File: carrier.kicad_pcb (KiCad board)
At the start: 4 copper layers, 20.3 x 68.6 mm, 29 parts, among them J1 Conn_02x06_Odd_Even, J2 Conn_01x26, J3 Conn_01x26, U1 CARAVEL, U2 W25Q128JVS, U3 LP5907MFX-3.3, U4 LP5907MFX-1.8, U5 LP5907MFX-1.8, U6 LP5907MFX-3.3, X1 SG-5032CAN

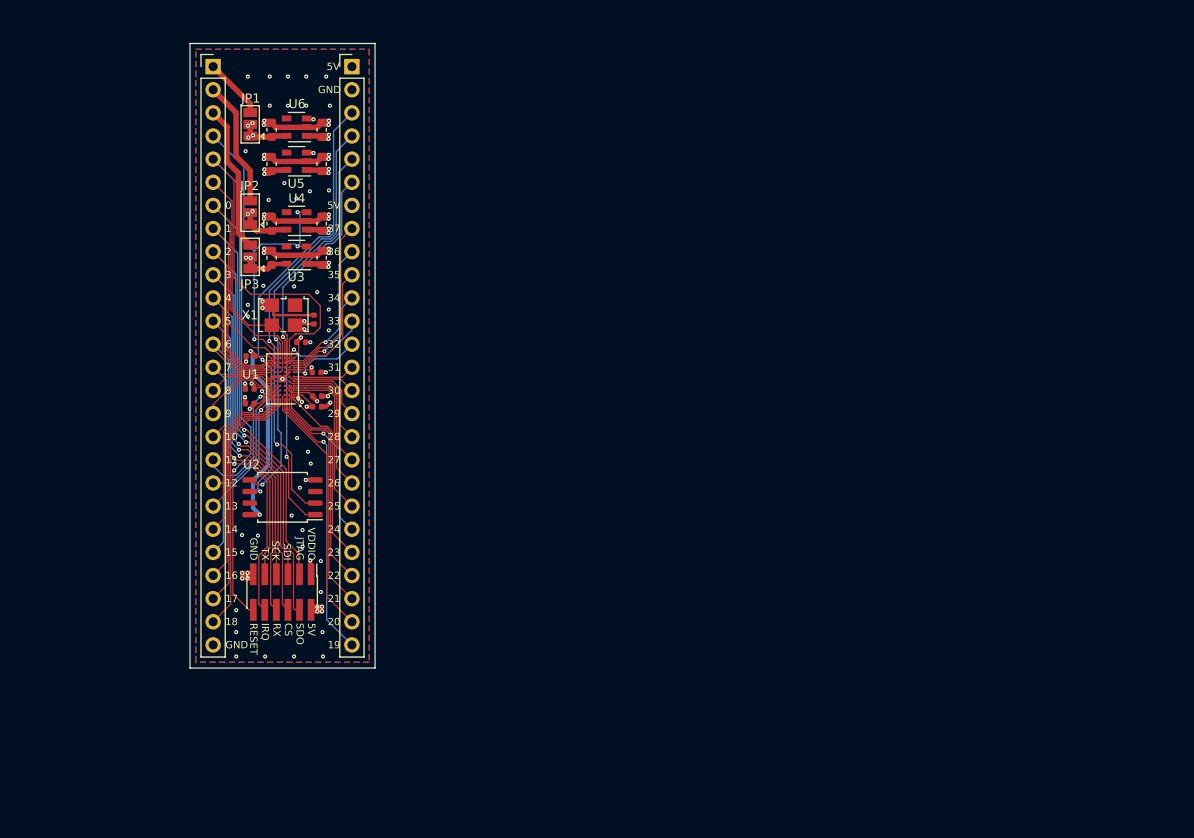
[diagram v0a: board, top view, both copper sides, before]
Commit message: Switch to 2.54mm header for programming
Also imports changes from schematic to PCB.
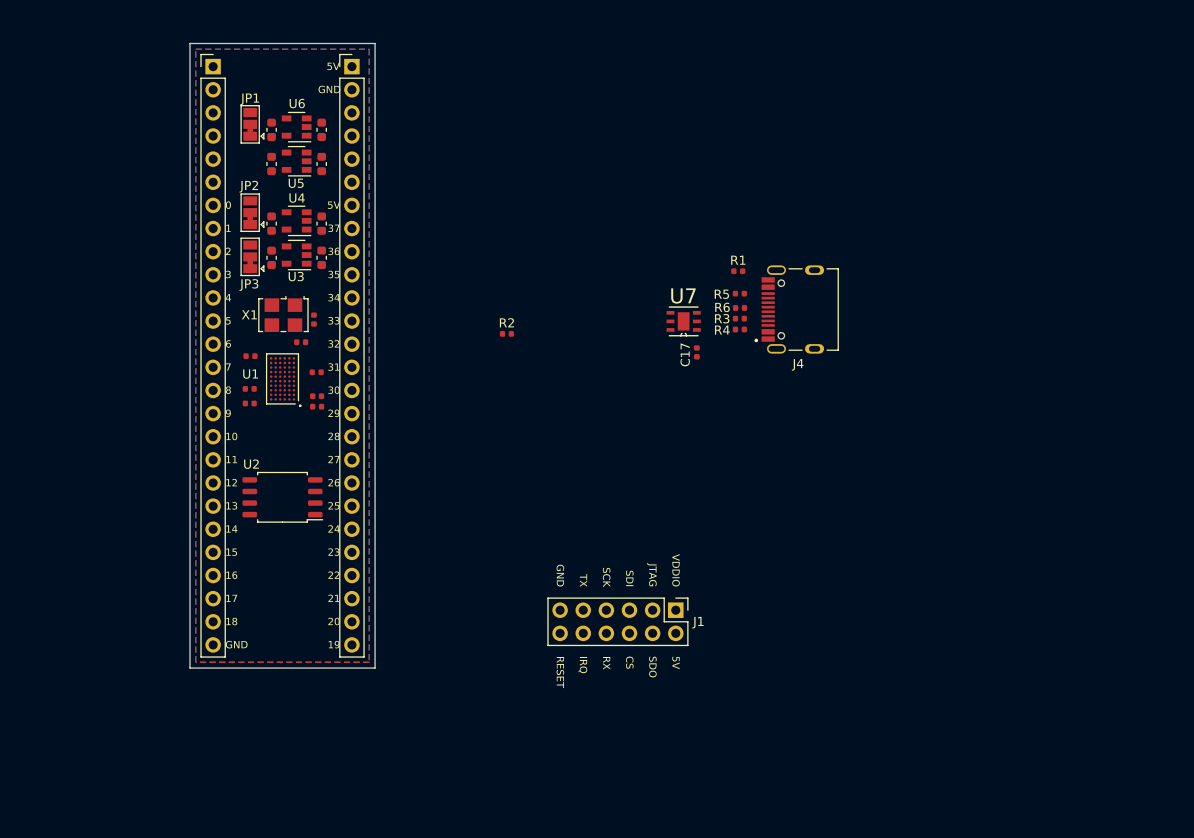
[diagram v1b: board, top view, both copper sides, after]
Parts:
- added C17: 22n, Capacitor_SMD:C_0402_1005Metric, F.Cu at (114.2, 77.1)
- added J4: TYPE-C-31-M-12, HRO_TYPE-C-31-M-12:HRO_TYPE-C-31-M-12, F.Cu at (127.2, 72.4)
- added R1: 1M Ohm, Resistor_SMD:R_0402_1005Metric, F.Cu at (118.8, 68.2)
- added R2: 22 Ohm, Resistor_SMD:R_0402_1005Metric, F.Cu at (93.4, 75.1)
- added R3: 22 Ohm, Resistor_SMD:R_0402_1005Metric, F.Cu at (118.9, 73.4)
- added R4: 5k1 Ohm, Resistor_SMD:R_0402_1005Metric, F.Cu at (118.9, 74.6)
- added R5: 5k1 Ohm, Resistor_SMD:R_0402_1005Metric, F.Cu at (118.9, 70.6)
- added R6: 1.5k Ohm, Resistor_SMD:R_0402_1005Metric, F.Cu at (119.0, 72.2)
- added U7: TPD2E001DRSR, TPD2E001DRSR:SON95P315X315X80-7N, F.Cu at (112.8, 73.7)
- J1: footprint Connector_PinHeader_1.27mm:PinHeader_2x06_P1.27mm_Vertical_SMD -> Connector_PinHeader_2.54mm:PinHeader_2x06_P2.54mm_Vertical
- moved J1 43.3 mm to (111.9, 105.4)
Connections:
- U1 pad D3: mprj_io[13] -> usb_pu
- U1 pad E3: mprj_io[11] -> usb_dn
- U1 pad F3: mprj_io[12] -> usb_dp
- U2 pad 3: no_connect_58 -> unconnected-(U2-Pad3)
- U2 pad 7: no_connect_59 -> unconnected-(U2-Pad7)
- U3 pad 4: no_connect_60 -> unconnected-(U3-Pad4)
- U4 pad 4: no_connect_61 -> unconnected-(U4-Pad4)
- U5 pad 4: no_connect_62 -> unconnected-(U5-Pad4)
- U6 pad 4: no_connect_63 -> unconnected-(U6-Pad4)
- X1 pad 1: no_connect_64 -> unconnected-(X1-Pad1)
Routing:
- net +5V: track 93.3 -> 0.00 mm, vias 14 -> 0
- net resetb: track 86.3 -> 0.00 mm, vias 1 -> 0
- net vdda: track 76.0 -> 0.00 mm, vias 6 -> 0
- net mprj_io[0]: track 67.5 -> 0.00 mm, vias 1 -> 0
- net mprj_io[1]: track 64.7 -> 0.00 mm, vias 1 -> 0
- net GND: track 61.9 -> 0.00 mm, vias 74 -> 0
- net vddio: track 58.0 -> 0.00 mm, vias 4 -> 0
- net mprj_io[2]: track 56.0 -> 0.00 mm, vias 1 -> 0
- net mprj_io[3]: track 55.9 -> 0.00 mm, vias 1 -> 0
- net flash_clk: track 51.4 -> 0.00 mm, vias 2 -> 0
- net flash_io1: track 50.6 -> 0.00 mm, vias 2 -> 0
- net mprj_io[4]: track 46.2 -> 0.00 mm, vias 1 -> 0
- net mprj_io[5]: track 46.1 -> 0.00 mm, vias 1 -> 0
- net flash_io0: track 44.8 -> 0.00 mm, vias 2 -> 0
- net flash_csb: track 44.6 -> 0.00 mm, vias 2 -> 0
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
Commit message: Update caravel ASIC footprint
It was mirrored about the Y-axis.

Thanks to Tim Edwards and Matt Venn for flagging this issue.
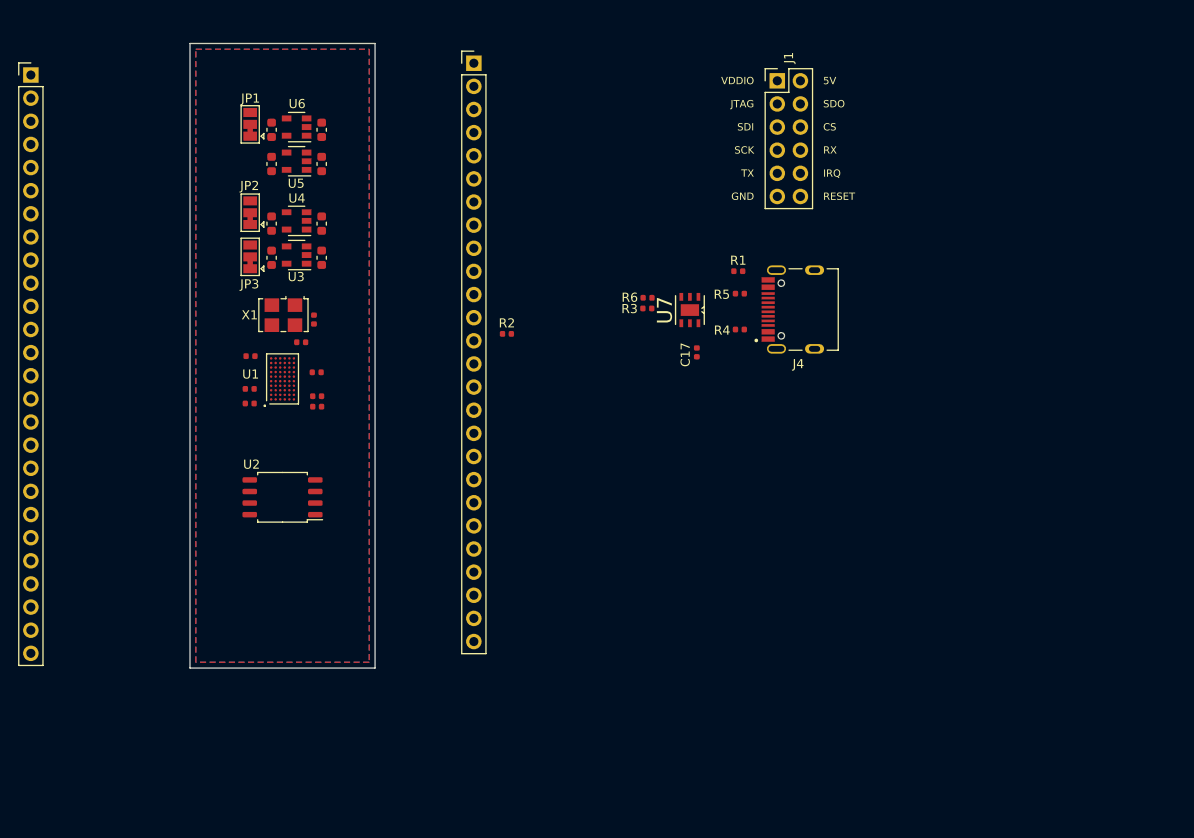
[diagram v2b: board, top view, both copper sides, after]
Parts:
- moved J1 59.2 mm to (123.1, 47.3), turned to 0 degrees
- moved J3 35.3 mm to (41.1, 46.6)
- moved J2 28.6 mm to (89.7, 45.3)
- moved R3 10.2 mm to (108.8, 72.3)
- moved R6 10.2 mm to (108.8, 71.1)
- moved U7 1.42 mm to (113.5, 72.4), turned to -90 degrees
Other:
- board text removed: "0"
- board text removed: "1"
- board text removed: "10"
- board text removed: "11"
- board text removed: "12"
- board text removed: "13"
- board text removed: "14"
- board text removed: "15"
- board text removed: "16"
- board text removed: "17"
- board text removed: "18"
- board text removed: "19"
- board text removed: "2"
- board text removed: "20"
- board text removed: "21"
- board text removed: "22"
- board text removed: "23"
- board text removed: "24"
- board text removed: "25"
- board text removed: "26"
- board text removed: "27"
- board text removed: "28"
- board text removed: "29"
- board text removed: "3"
- board text removed: "30"
- board text removed: "31"
- board text removed: "32"
- board text removed: "33"
- board text removed: "34"
- board text removed: "35"
- board text removed: "36"
- board text removed: "37"
- board text removed: "4"
- board text removed: "5"
- board text removed: "6"
- board text removed: "7"
- board text removed: "8"
- board text removed: "9"

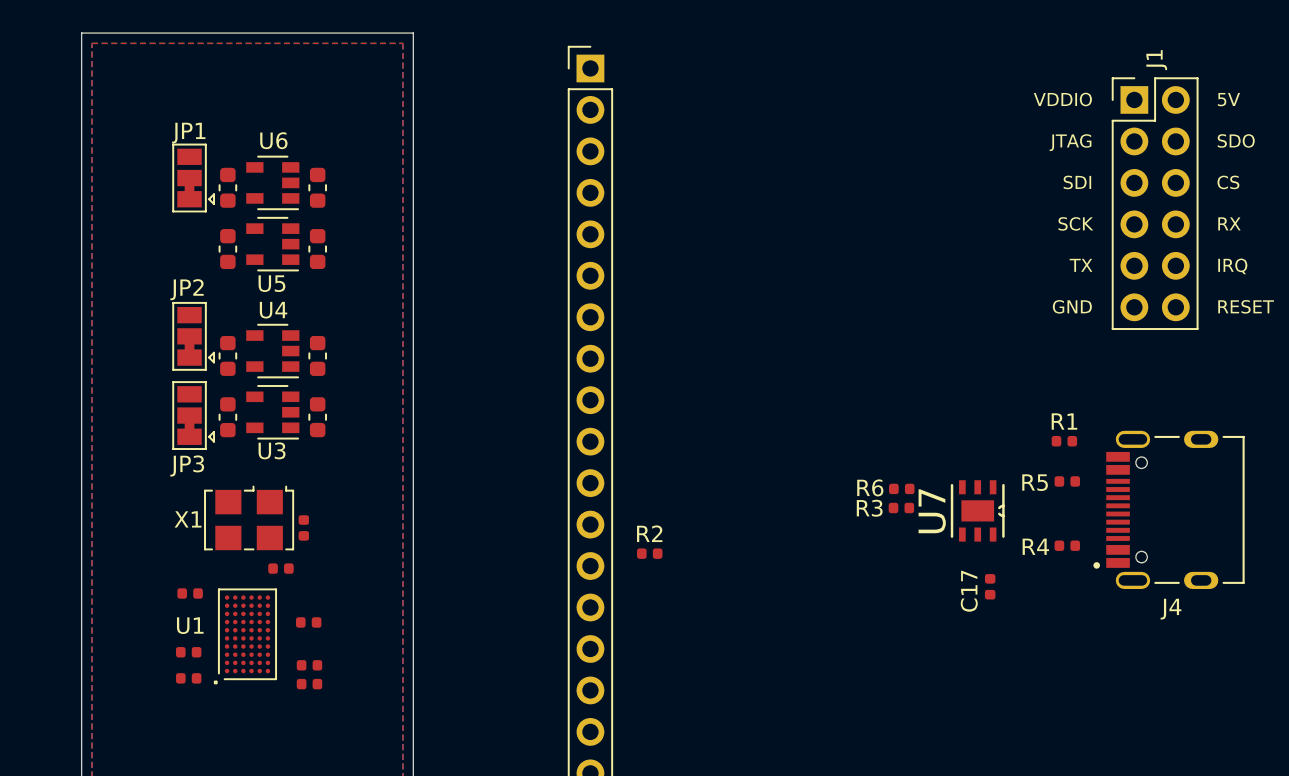
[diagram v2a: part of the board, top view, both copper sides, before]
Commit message: Add current measurement jumpers
Removes solder bridges and adds jumpers for each power rail to measure current.
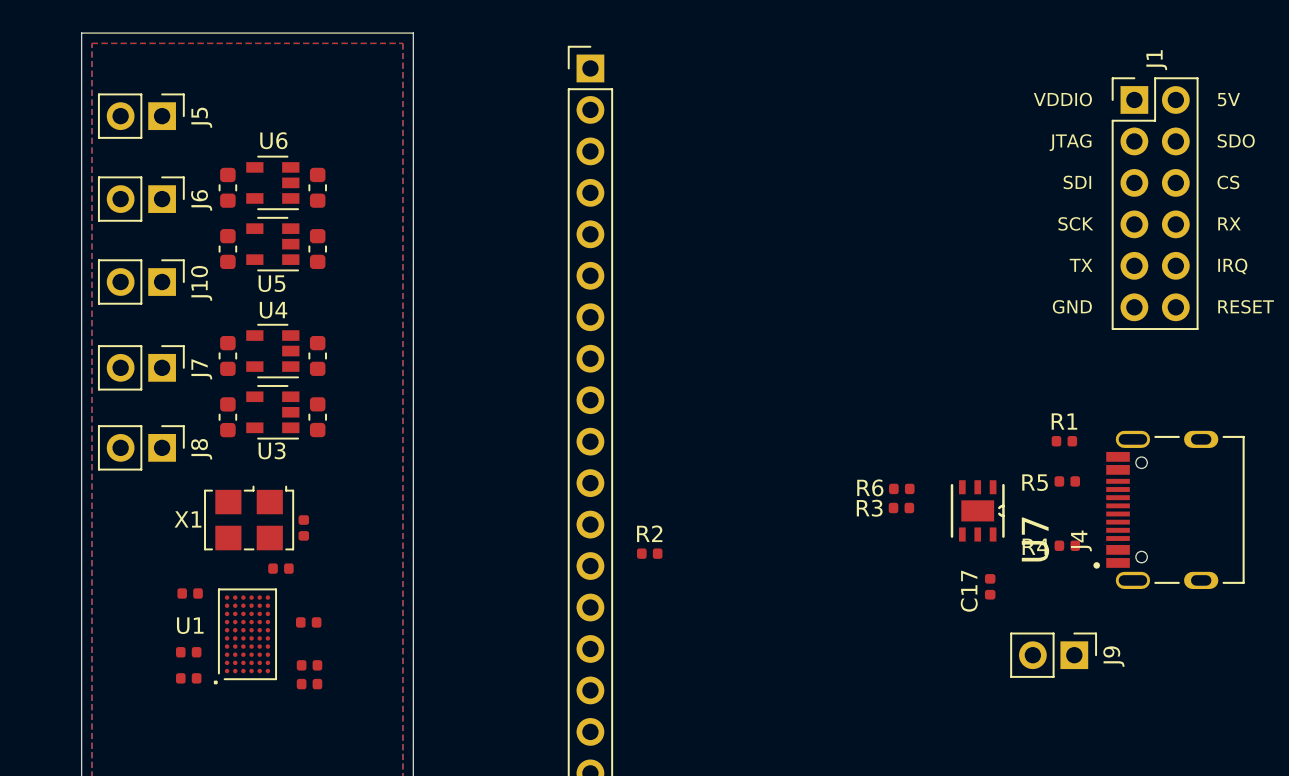
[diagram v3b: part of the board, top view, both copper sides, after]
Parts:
- removed JP1: VIO_SEL, Jumper:SolderJumper-3_P1.3mm_Bridged12_Pad1.0x1.5mm
- removed JP2: 1V8_SEL, Jumper:SolderJumper-3_P1.3mm_Bridged12_Pad1.0x1.5mm
- removed JP3: 3V3_SEL, Jumper:SolderJumper-3_P1.3mm_Bridged12_Pad1.0x1.5mm
- added J10: Conn_01x02, Connector_PinHeader_2.54mm:PinHeader_1x02_P2.54mm_Vertical, F.Cu at (63.5, 58.4)
- added J5: Conn_01x02, Connector_PinHeader_2.54mm:PinHeader_1x02_P2.54mm_Vertical, F.Cu at (63.5, 48.3)
- added J6: Conn_01x02, Connector_PinHeader_2.54mm:PinHeader_1x02_P2.54mm_Vertical, F.Cu at (63.5, 53.3)
- added J7: Conn_01x02, Connector_PinHeader_2.54mm:PinHeader_1x02_P2.54mm_Vertical, F.Cu at (63.5, 63.7)
- added J8: Conn_01x02, Connector_PinHeader_2.54mm:PinHeader_1x02_P2.54mm_Vertical, F.Cu at (63.5, 68.6)
- added J9: Conn_01x02, Connector_PinHeader_2.54mm:PinHeader_1x02_P2.54mm_Vertical, F.Cu at (119.4, 81.3)
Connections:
- C3 pad 1: vccd -> Net-(C3-Pad1)
- C7 pad 1: vdda -> Net-(C7-Pad1)
- J2 pad 1: ext_vddio -> unconnected-(J2-Pad1)
- J2 pad 2: ext_1v8 -> unconnected-(J2-Pad2)
- J2 pad 3: ext_3v3 -> unconnected-(J2-Pad3)
- J4 pad A4B9: +5V -> Net-(J4-PadA4B9)
- J4 pad B4A9: +5V -> Net-(J4-PadA4B9)
- U5 pad 5: vccd -> Net-(C3-Pad1)
- U6 pad 5: vdda -> Net-(C7-Pad1)
